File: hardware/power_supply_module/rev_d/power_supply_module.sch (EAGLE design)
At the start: 171 parts, among them J1 MODULE_POWER, J3 TC2030-CTX-NL, Q1 MOSFET-NCHANNELFDD8580, U1 TLV62130, U10 LTC2943, U11 LTC2943, U12 LTC2943, U13 LTC2943, U14 LTC2943, U15 LTC2943, U16 LT3652, U17 LM234, U18 MAX17205, U19 ESDR0502N, U2 TLV62130, U20 AP22814, U21 AP22814, U22 AP22814, U23 AP22814, U24 AP22814, U25 PCA9544AQFN-N20, U26 LTC2943, U27 MAX6746, U28 3.3V, U29 M24C01WMN, U3 TLV62130, U4 TLV62130, U5 TLV62130, U6 PCA9544AQFN-N20, U7 PCA9544AQFN-N20, U8 LTC2941, U9 LTC2943

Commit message: reroute watchdog and move labels
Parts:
- U28: DIGIKEY (none) -> ZMR330FCT-ND
- renumbered CHRG_FAULT to FAULT, VBATT-M to MON_GND
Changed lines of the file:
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@@
 <attribute name="DIGIKEY" value="490-10440-1-ND"/>
 </part>
-<part name="U28" library="chips" deviceset="TILM3480" device="" technology="3.3V" value="3.3V"/>
+<part name="U28" library="chips" deviceset="TILM3480" device="" technology="3.3V" value="3.3V">
+<attribute name="DIGIKEY" value="ZMR330FCT-ND"/>
+</part>
 <part name="C21" library="passives" deviceset="CAPACITOR" device="0402_CAP" value="0.1 uF">
 <attribute name="DIGIKEY" value="490-5920-1-ND "/>
@@
 <part name="FRAME7" library="lab11-frames" deviceset="LETTER_L_BLANK" device=""/>
 <part name="U27" library="chips" deviceset="MAX6746" device=""/>
-<part name="VBATT-M" library="headers" deviceset="TEST_POINT_0.040IN" device=""/>
+<part name="MON_GND" library="headers" deviceset="TEST_POINT_0.040IN" device=""/>
 <part name="FRAME8" library="lab11-frames" deviceset="LETTER_L_BLANK" device=""/>
 <part name="U29" library="chips" deviceset="M24C01" device="WMN"/>
@@
 </part>
 <part name="U$47" library="signpost" deviceset="VCC_BACKPLANE" device=""/>
-<part name="CHRG_FAULT" library="headers" deviceset="TEST_POINT_0.040IN" device=""/>
+<part name="FAULT" library="headers" deviceset="TEST_POINT_0.040IN" device=""/>
 <part name="CHRG" library="headers" deviceset="TEST_POINT_0.040IN" device=""/>
 </parts>
@@
 <instance part="5V_3" gate="G$1" x="116.84" y="119.38"/>
 <instance part="5V_4" gate="G$1" x="116.84" y="116.84"/>
-<instance part="VBATT-M" gate="G$1" x="116.84" y="132.08"/>
+<instance part="MON_GND" gate="G$1" x="116.84" y="132.08"/>
 <instance part="J3" gate="G$1" x="121.92" y="73.66"/>
 <instance part="JP1" gate="G$1" x="114.3" y="88.9"/>
-<instance part="CHRG_FAULT" gate="G$1" x="116.84" y="111.76"/>
+<instance part="FAULT" gate="G$1" x="116.84" y="111.76"/>
 <instance part="CHRG" gate="G$1" x="116.84" y="109.22"/>
 </instances>
@@
 <net name="MONITOR_GND" class="0">
 <segment>
-<pinref part="VBATT-M" gate="G$1" pin="TESTPOINT"/>
+<pinref part="MON_GND" gate="G$1" pin="TESTPOINT"/>
 <wire x1="119.38" y1="132.08" x2="121.92" y2="132.08" width="0.1524" layer="91"/>
 <label x="121.92" y="132.08" size="1.27" layer="95" xref="yes"/>
@@
 <net name="CHRG_FAULT" class="0">
 <segment>
-<pinref part="CHRG_FAULT" gate="G$1" pin="TESTPOINT"/>
+<pinref part="FAULT" gate="G$1" pin="TESTPOINT"/>
 <wire x1="119.38" y1="111.76" x2="121.92" y2="111.76" width="0.1524" layer="91"/>
 <label x="121.92" y="111.76" size="1.27" layer="95" xref="yes"/>

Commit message: change pogo pin device/symbol
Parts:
- J3: value TC2030-CTX-NL -> TC2030-FTDI-I2C; device connector:TC2030-CTX-NL -> connector:TC2030-FTDI-I2C
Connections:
- net GND: now also J3.GND; no longer J3.!RESET
- net SCL: now also J3.SCL; no longer J3.VCC
- net SDA: now also J3.SDA; no longer J3.GND
- net VCC_BACKPLANE: now also J3.VCC; no longer J3.TDO
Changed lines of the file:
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@@
 <attributes>
 <attribute name="AUTHOR" value="N. Jackson"/>
-<attribute name="REV" value="A"/>
+<attribute name="REV" value="D"/>
 <attribute name="TITLE" value="Power Supply Module"/>
 </attributes>
@@
 <part name="H3" library="holes" deviceset="MOUNT-PAD-ROUND" device="3.0"/>
 <part name="H4" library="holes" deviceset="MOUNT-PAD-ROUND" device="3.0"/>
-<part name="J3" library="connector" deviceset="TC2030-CTX" device="-NL"/>
+<part name="J3" library="connector" deviceset="TC2030-FTDI-I2C" device=""/>
 <part name="JP1" library="SparkFun-Connectors" deviceset="M04" device="PTH"/>
 <part name="U$2" library="signpost" deviceset="VCC_MOD0" device=""/>
@@
 <instance part="5V_4" gate="G$1" x="116.84" y="116.84"/>
 <instance part="MON_GND" gate="G$1" x="116.84" y="132.08"/>
-<instance part="J3" gate="G$1" x="121.92" y="73.66"/>
+<instance part="J3" gate="G$1" x="121.92" y="71.12"/>
 <instance part="JP1" gate="G$1" x="114.3" y="88.9"/>
 <instance part="FAULT" gate="G$1" x="116.84" y="111.76"/>
@@
 </segment>
 </net>
-<net name="SCL" class="0">
-<segment>
-<pinref part="J3" gate="G$1" pin="VCC"/>
-<wire x1="109.22" y1="76.2" x2="106.68" y2="76.2" width="0.1524" layer="91"/>
-<label x="106.68" y="76.2" size="1.27" layer="95" rot="R180" xref="yes"/>
-</segment>
-</net>
-<net name="SDA" class="0">
-<segment>
-<pinref part="J3" gate="G$1" pin="GND"/>
-<wire x1="109.22" y1="68.58" x2="106.68" y2="68.58" width="0.1524" layer="91"/>
-<label x="106.68" y="68.58" size="1.27" layer="95" rot="R180" xref="yes"/>
-</segment>
-</net>
-<net name="VCC_BACKPLANE" class="0">
-<segment>
-<pinref part="J3" gate="G$1" pin="TDO"/>
-<wire x1="134.62" y1="71.12" x2="137.16" y2="71.12" width="0.1524" layer="91"/>
-<label x="137.16" y="71.12" size="1.27" layer="95" xref="yes"/>
-</segment>
-</net>
 <net name="GND" class="0">
 <segment>
-<pinref part="J3" gate="G$1" pin="!RESET"/>
-<wire x1="134.62" y1="68.58" x2="137.16" y2="68.58" width="0.1524" layer="91"/>
-<label x="137.16" y="68.58" size="1.27" layer="95" xref="yes"/>
-</segment>
-<segment>
 <pinref part="JP1" gate="G$1" pin="1"/>
 <wire x1="119.38" y1="86.36" x2="121.92" y2="86.36" width="0.1524" layer="91"/>
 <label x="121.92" y="86.36" size="1.27" layer="95" xref="yes"/>
 </segment>
+<segment>
+<pinref part="J3" gate="G$1" pin="GND"/>
+<wire x1="111.76" y1="68.58" x2="109.22" y2="68.58" width="0.1524" layer="91"/>
+<label x="109.22" y="68.58" size="1.27" layer="95" rot="R180" xref="yes"/>
+</segment>
 </net>
 <net name="VBAT-" class="0">
@@
 </segment>
 </net>
+<net name="VCC_BACKPLANE" class="0">
+<segment>
+<pinref part="J3" gate="G$1" pin="VCC"/>
+<wire x1="111.76" y1="73.66" x2="109.22" y2="73.66" width="0.1524" layer="91"/>
+<label x="109.22" y="73.66" size="1.27" layer="95" rot="R180" xref="yes"/>
+</segment>
+</net>
+<net name="SCL" class="0">
+<segment>
+<pinref part="J3" gate="G$1" pin="SCL"/>
+<wire x1="132.08" y1="73.66" x2="134.62" y2="73.66" width="0.1524" layer="91"/>
+<label x="134.62" y="73.66" size="1.27" layer="95" xref="yes"/>
+</segment>
+</net>
+<net name="SDA" class="0">
+<segment>
+<pinref part="J3" gate="G$1" pin="SDA"/>
+<wire x1="132.08" y1="68.58" x2="134.62" y2="68.58" width="0.1524" layer="91"/>
+<label x="134.62" y="68.58" size="1.27" layer="95" xref="yes"/>
+</segment>
+</net>

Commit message: move more labels
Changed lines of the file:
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@@
 <schematic xreflabel="%F%N/%S" xrefpart="/%S">
 <attributes>
-<attribute name="AUTHOR" value="N. Jackson"/>
+<attribute name="AUTHOR" value="Neal Jackson"/>
 <attribute name="REV" value="D"/>
 <attribute name="TITLE" value="Power Supply Module"/>

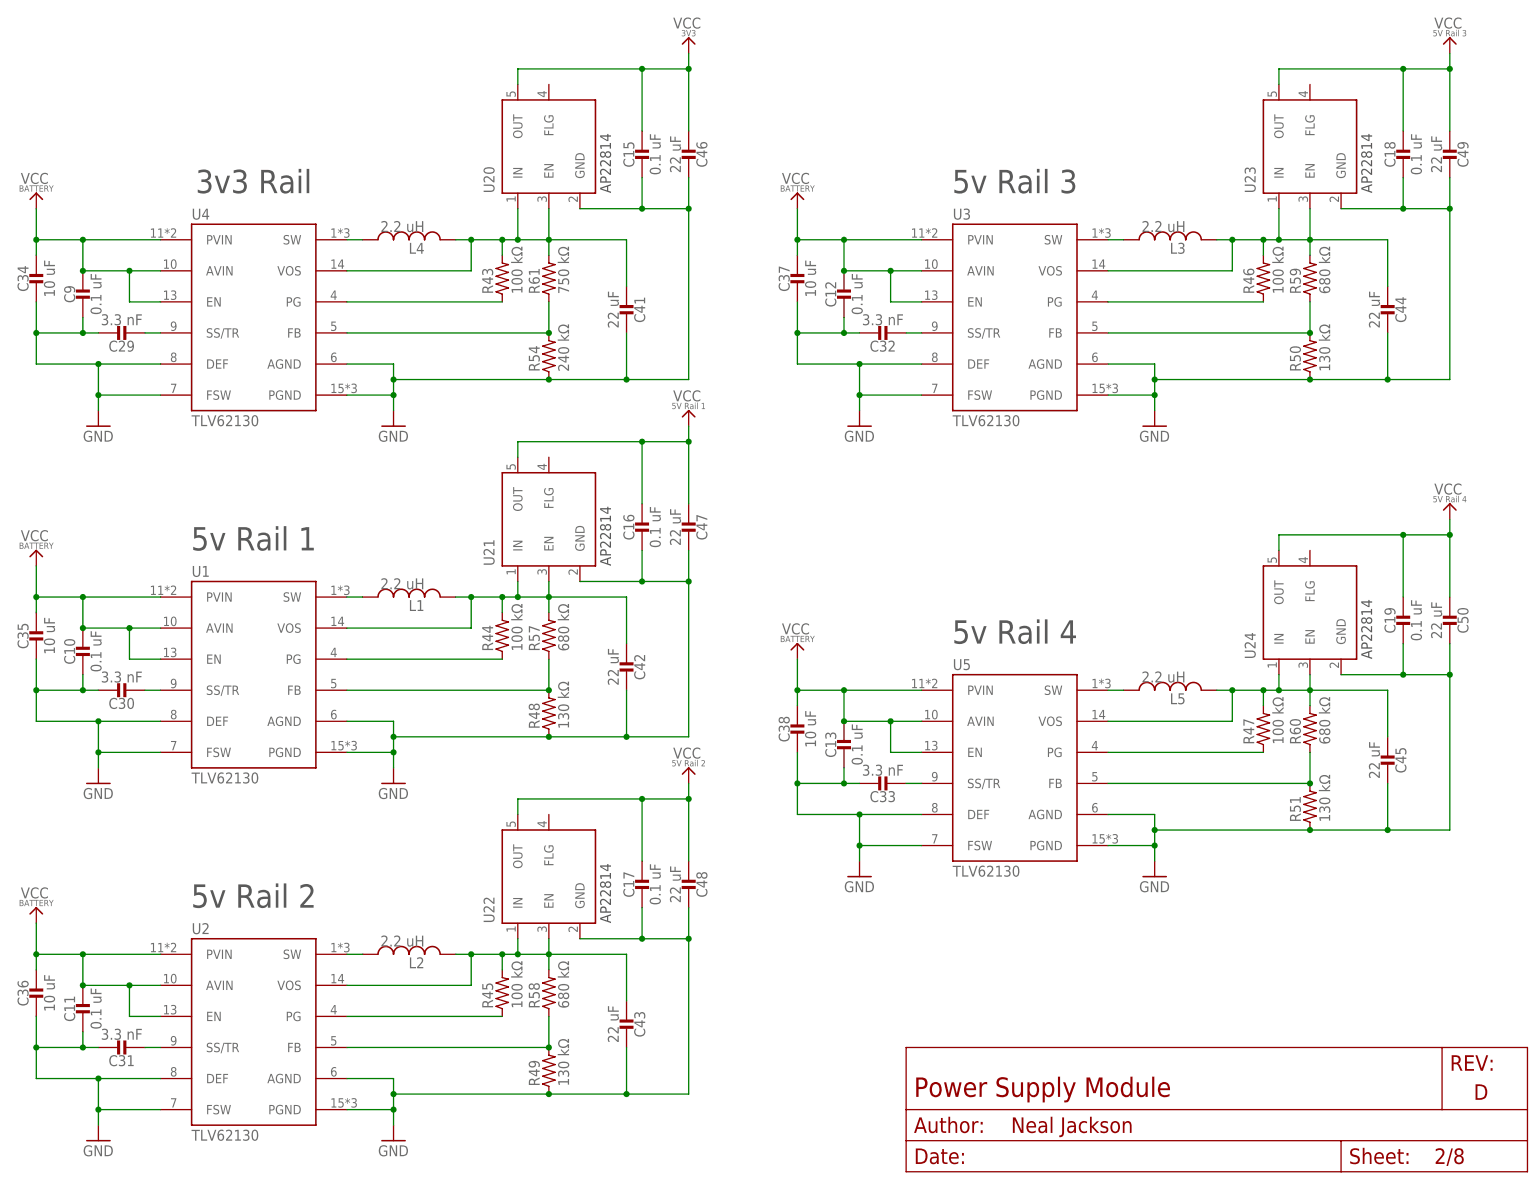
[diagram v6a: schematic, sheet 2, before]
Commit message: rename passives, fix silk
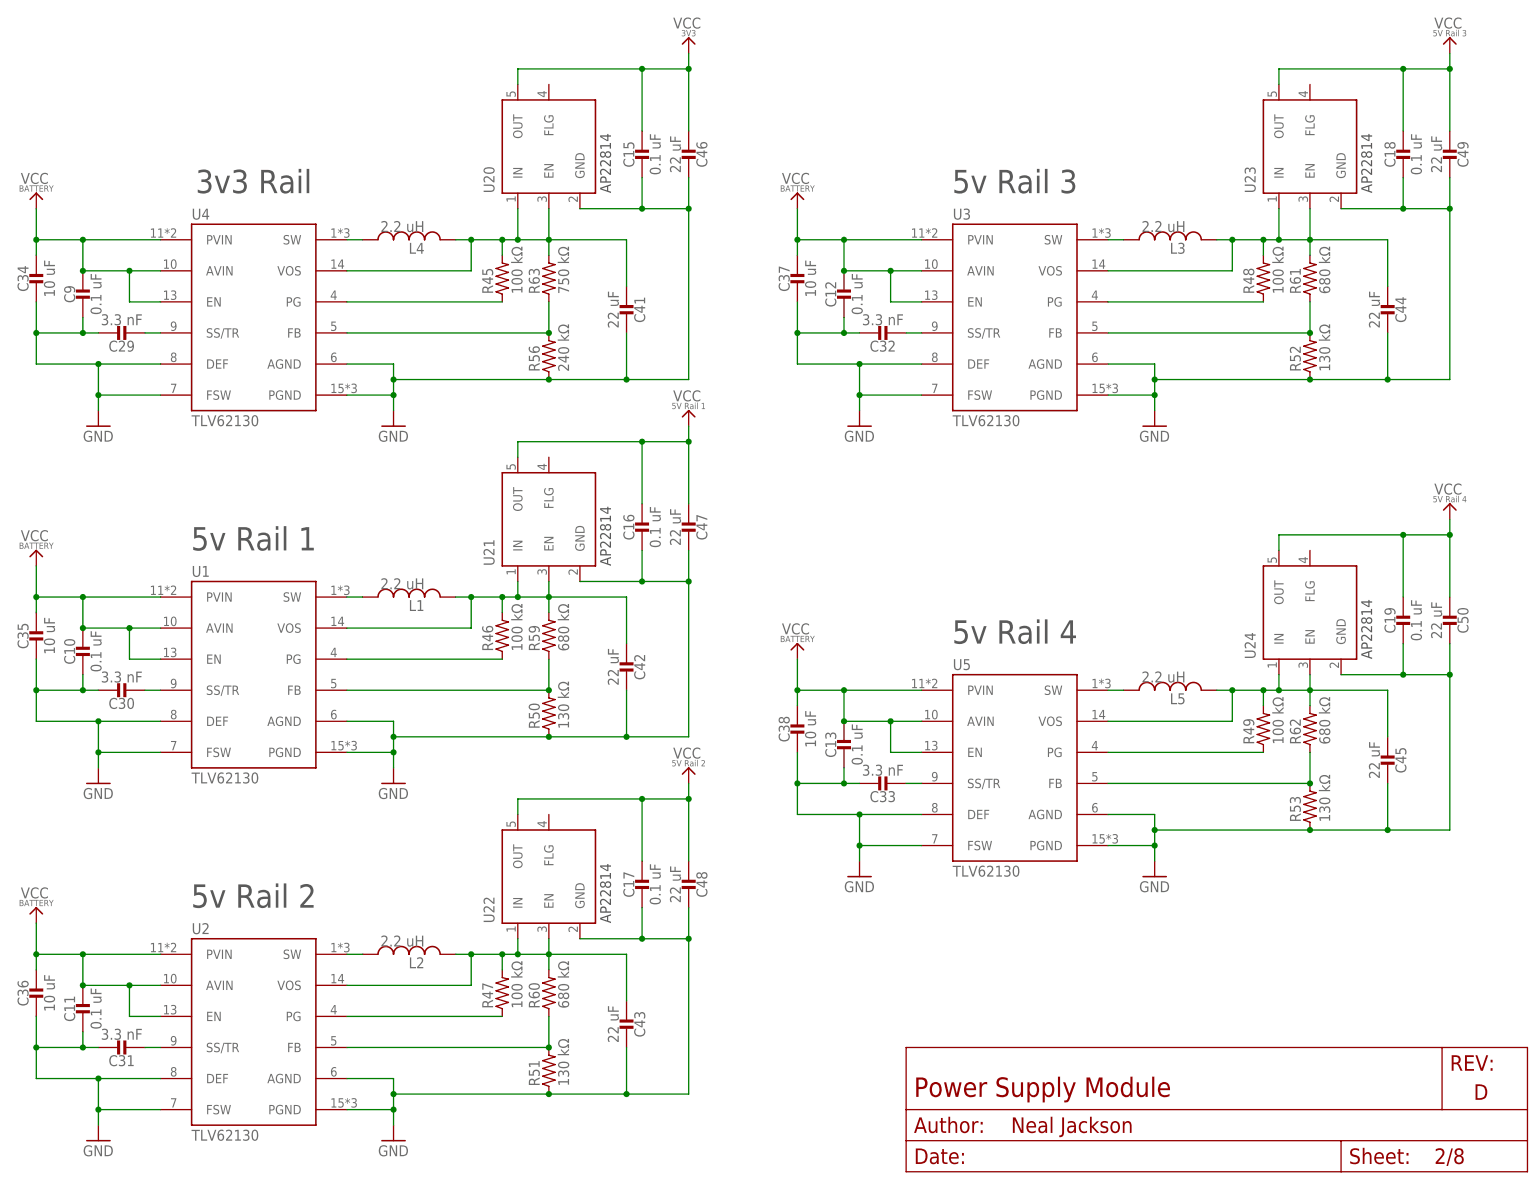
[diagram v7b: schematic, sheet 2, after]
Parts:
- R13: value 150 Ω -> 1 kΩ; DIGIKEY P1.0KJCT-ND -> P150LCT-ND
- R15, R16: value 2 kΩ -> 1 MΩ; DIGIKEY P2.00KLCT-ND -> P1.0KJCT-ND
- R42: value 23.2 kΩ -> 2 kΩ; device passives:RESISTOR0805_RES -> passives:RESISTOR0402_RES; DIGIKEY P23.2KDATR-ND -> P2.00KLCT-ND
- R43: value 100 kΩ -> 2 kΩ; DIGIKEY P100KJCT-ND -> P2.00KLCT-ND
- R44: value 100 kΩ -> 23.2 kΩ; device passives:RESISTOR0402_RES -> passives:RESISTOR0805_RES; DIGIKEY P100KJCT-ND -> P23.2KDATR-ND
- R48, R49: value 130 kΩ -> 100 kΩ; DIGIKEY P130KLCT-ND -> P100KJCT-ND
- R52: value 150 Ω -> 130 kΩ; DIGIKEY P150LCT-ND -> P130KLCT-ND
- R53: value 1 kΩ -> 130 kΩ; DIGIKEY P150LCT-ND -> P130KLCT-ND
- R54: value 240 kΩ -> 150 Ω; DIGIKEY P240KLCT-ND -> P1.0KJCT-ND
- R55: value 301 kΩ -> 150 Ω; device passives:RESISTOR0805_RES -> passives:RESISTOR0402_RES; DIGIKEY P301KDATR-ND -> P150LCT-ND
- R56: value 340 kΩ -> 240 kΩ; device passives:RESISTOR0805_RES -> passives:RESISTOR0402_RES; DIGIKEY P340KDACT-ND -> P240KLCT-ND
- R57: value 680 kΩ -> 301 kΩ; device passives:RESISTOR0402_RES -> passives:RESISTOR0805_RES; DIGIKEY P680KLCT-ND -> P301KDATR-ND
- R58: value 680 kΩ -> 340 kΩ; device passives:RESISTOR0402_RES -> passives:RESISTOR0805_RES; DIGIKEY P680KLCT-ND -> P340KDACT-ND
- R61: value 750 kΩ -> 680 kΩ; DIGIKEY P750KJCT-ND -> P680KLCT-ND
- R62: value 953 kΩ -> 680 kΩ; device passives:RESISTOR0805_RES -> passives:RESISTOR0402_RES; DIGIKEY P953KDACT-ND -> P680KLCT-ND
- R63: value 1 MΩ -> 750 kΩ; DIGIKEY P1.0KJCT-ND -> P750KJCT-ND
- R64: value 1 MΩ -> 953 kΩ; device passives:RESISTOR0402_RES -> passives:RESISTOR0805_RES; DIGIKEY P1.0KJCT-ND -> P953KDACT-ND
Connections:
- net !INT: now also R13.2; no longer R53.2
- net 3V3ROUT: now also R45.2, R63.2; no longer R43.2, R61.2
- net 5V_1ROUT: now also R46.2, R59.2; no longer R44.2, R57.2
- net 5V_2ROUT: now also R47.2, R60.2; no longer R45.2, R58.2
- net 5V_3ROUT: now also R48.2, R61.2; no longer R46.2, R59.2
- net 5V_4ROUT: now also R49.2, R62.2; no longer R47.2, R60.2
- net CHRG: now also R16.1; no longer R64.1
- net CHRG_FAULT: now also R15.1; no longer R63.1
- net GND: now also R52.1, R53.1, R56.1; no longer R48.1, R49.1, R54.1
- net MONITOR_GND: now also R44.1, R58.2; no longer R42.1, R56.2
- net N$10: now also R47.1; no longer R45.1
- net N$11: now also R51.2, R60.1; no longer R49.2, R58.1
- net N$18: now also R45.1; no longer R43.1
- net N$19: now also R56.2, R63.1; no longer R54.2, R61.1
- net N$21: now also R35.1; no longer R33.1
- net N$22: now also R36.1; no longer R34.1
- net N$23: now also R29.1; no longer R27.1
- net N$24: now also R30.1; no longer R28.1
- net N$25: now also R31.1; no longer R29.1
- net N$26: now also R38.1; no longer R36.1
- net N$27: now also R39.1; no longer R37.1
- net N$30: now also R48.1; no longer R46.1
- net N$31: now also R52.2, R61.1; no longer R50.2, R59.1
- net N$36: now also R49.1; no longer R47.1
- net N$37: now also R53.2, R62.1; no longer R51.2, R60.1
- net N$42: now also R54.1; no longer R13.1
- net N$43: now also R17.1; no longer R15.1
- net N$46: now also R40.1; no longer R38.1
- net N$47: now also R18.1; no longer R16.1
- net N$48: now also R37.1; no longer R35.1
- net N$49: now also R32.1; no longer R30.1
- net N$5: now also R46.1; no longer R44.1
- net N$50: now also R33.1; no longer R31.1
- net N$51: now also R34.1; no longer R32.1
- net N$52: now also R23.1; no longer R21.1
- net N$53: now also R24.1; no longer R22.1
- net N$54: now also R25.1; no longer R23.1
- net N$55: now also R26.1; no longer R24.1
- net N$56: now also R27.1; no longer R25.1
- net N$57: now also R28.1; no longer R26.1
- net N$58: now also R55.1; no longer R52.1
- net N$6: now also R50.2, R59.1; no longer R48.2, R57.1
- net N$61: now also R13.1; no longer R53.1
- net N$67: now also R19.1; no longer R17.1
- net N$68: now also R20.1; no longer R18.1
- net N$70: now also R21.1; no longer R19.1
- net N$71: now also R22.1; no longer R20.1
- net N$73: now also R43.1; no longer R41.1
- net N$74: now also R42.1; no longer R40.1
- net N$75: now also R41.1; no longer R39.1
- net SCL: now also R55.2; no longer R52.2
- net SDA: now also R54.2; no longer R13.2
- net VBAT+: now also R64.2; no longer R62.2
- net VCC_3V3: now also R18.2, R19.2; no longer R15.2, R16.2
- net VCC_5V_1: now also R21.2, R22.2; no longer R18.2, R19.2
- net VCC_5V_2: now also R27.2, R28.2; no longer R21.2, R22.2
- net VCC_5V_3: now also R36.2, R37.2; no longer R30.2, R31.2
- net VCC_5V_4: now also R30.2, R31.2, R39.2, R40.2; no longer R27.2, R28.2, R36.2, R37.2
- net VCC_BACKPLANE: now also R15.2, R16.2, R42.2, R43.2; no longer R39.2, R40.2, R63.2, R64.2
- net VFB: now also R58.1, R64.1; no longer R56.1, R62.1
- net VINREG: now also R44.2, R57.1; no longer R42.2, R55.1
- net VSOL_SENSE: now also R57.2; no longer R55.2
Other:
- moved on the sheet: R13, R17, R18, R19, R20, R21, R22, R23, R24, R25, R26, R29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

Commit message: fix some part number attributes
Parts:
- R13: DIGIKEY P150LCT-ND -> P1.0KJCT-ND
- R15, R16: DIGIKEY P1.0KJCT-ND -> P1.00MLCT-ND
- R44: DIGIKEY P23.2KDATR-ND -> P23.2KDACT-ND
- R54: DIGIKEY P1.0KJCT-ND -> P150LCT-ND
- R57: DIGIKEY P301KDATR-ND -> P301KDACT-ND
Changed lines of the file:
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@@
 </part>
 <part name="R57" library="passives" deviceset="RESISTOR" device="0805_RES" value="301 kΩ">
-<attribute name="DIGIKEY" value="P301KDATR-ND"/>
+<attribute name="DIGIKEY" value="P301KDACT-ND"/>
 </part>
 <part name="R44" library="passives" deviceset="RESISTOR" device="0805_RES" value="23.2 kΩ">
-<attribute name="DIGIKEY" value="P23.2KDATR-ND"/>
+<attribute name="DIGIKEY" value="P23.2KDACT-ND"/>
 </part>
 <part name="C40" library="passives" deviceset="CAPACITOR" device="0805_CAP" value="10 uF">
@@
 </part>
 <part name="R54" library="passives" deviceset="RESISTOR" device="0402_RES" value="150 Ω">
-<attribute name="DIGIKEY" value="P1.0KJCT-ND"/>
+<attribute name="DIGIKEY" value="P150LCT-ND"/>
 </part>
 <part name="R55" library="passives" deviceset="RESISTOR" device="0402_RES" value="150 Ω">
@@
 </part>
 <part name="R13" library="passives" deviceset="RESISTOR" device="0402_RES" value="1 kΩ">
-<attribute name="DIGIKEY" value="P150LCT-ND"/>
+<attribute name="DIGIKEY" value="P1.0KJCT-ND"/>
 </part>
 <part name="C24" library="passives" deviceset="CAPACITOR" device="0402_CAP" value="0.47 uF">
@@
 <part name="GND13" library="signpost" deviceset="MONITOR_GND" device=""/>
 <part name="R15" library="passives" deviceset="RESISTOR" device="0402_RES" value="1 MΩ">
-<attribute name="DIGIKEY" value="P1.0KJCT-ND"/>
+<attribute name="DIGIKEY" value="P1.00MLCT-ND"/>
 </part>
 <part name="R16" library="passives" deviceset="RESISTOR" device="0402_RES" value="1 MΩ">
-<attribute name="DIGIKEY" value="P1.0KJCT-ND"/>
+<attribute name="DIGIKEY" value="P1.00MLCT-ND"/>
 </part>
 <part name="U$47" library="signpost" deviceset="VCC_BACKPLANE" device=""/>
